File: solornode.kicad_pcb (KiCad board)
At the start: 2 copper layers, 35.9 x 42.4 mm, 86 parts, among them J1 Conn_01x06, J2 Conn_01x02, J3 Conn_01x02, J4 Conn_01x02, Q1 Q_NMOS_GDS, Q4 Q_PNP_BCE, Q5 Q_NPN_BCE, SW1 SW_Push, U1 LM358, U2 OC5864, U3 PY32F003F1xUx, U4 MAX485E, U5 SGM2033-3.3

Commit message: 修改元器件参数
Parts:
- C1: value 100u -> 22uF 50V
- C12, C13: value 100nF -> 100nF 100V
- C16: value C -> 10uF
- C17, C9: value 10u -> 10uF
- C2, C4: value 10u -> 2.2uF 100V
- C3: value 100u -> 10uF 100V
- C5: value 0.1u -> 0.1uF
- C6, C7: value 4.7n -> 4.7nF
- C8: value 2.2u -> 1uF 100V
- D12, D13: value D -> DSF1D
- D2, D3: value D_Zener -> CESD3V3D5
- D5, D6, D7: value ESD5Zxx -> CESDB5V0D3
- FB1, FB2: value 30 -> 1000R
- GD1, GD2, GD3: value GDT_2Pin -> 75V
- L2: value 47u -> 47uH
- L3: value L_Coupled -> 1000R
- Q1: value Q_NMOS_GDS -> AO3400
- Q4: value Q_PNP_BCE -> S8550
- Q5: value Q_NPN_BCE -> S8050
- R20, R26, R27: value R -> 10k
- R21, R22: value 22 -> 22R
- R28: value 470 -> 470R
- SW1: value SW_Push -> 3*4*2mm
- U3: value PY32F003F1xUx -> PY32F003F18U6TR
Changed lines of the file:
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@@
 			)
 		)
-		(property "Value" "R"
+		(property "Value" "10k"
 			(at 0 1.17 0)
 			(layer "F.Fab")
@@
 			)
 		)
-		(property "Value" "PY32F003F1xUx"
+		(property "Value" "PY32F003F18U6TR"
 			(at 0 2.83 0)
 			(layer "F.Fab")
@@
 			)
 		)
-		(property "Datasheet" ""
+		(property "Datasheet" "https://www.puyasemi.com/download_path/%E6%95%B0%E6%8D%AE%E6%89%8B%E5%86%8C/MCU%20%E5%BE%AE%E5%A4%84%E7%90%86%E5%99%A8/PY32F003%E7%B3%BB%E5%88%97%E6%95%B0%E6%8D%AE%E6%89%8B%E5%86%8C_V2.7.pdf"
 			(at 0 0 0)
 			(layer "F.Fab")
@@
 		(sheetname "根目录")
 		(sheetfile "solornode.kicad_sch")
-		(attr smd)
+		(attr smd dnp)
 		(fp_line
 			(start -1.685 0.96)
@@
 			)
 		)
-		(property "Value" "GDT_2Pin"
+		(property "Value" "75V"
 			(at 0 1.85 90)
 			(layer "F.Fab")
@@
 			)
 		)
-		(property "Value" "470"
+		(property "Value" "470R"
 			(at 0 1.17 0)
 			(layer "F.Fab")
@@
 			)
 		)
-		(property "Value" "Q_NMOS_GDS"
+		(property "Value" "AO3400"
 			(at 0 2.4 0)
 			(layer "F.Fab")
@@
 			)
 		)
-		(property "Value" "ESD5Zxx"
+		(property "Value" "CESDB5V0D3"
 			(at 0.1 1.9 0)
 			(layer "F.Fab")
@@
 			)
 		)
-		(property "Datasheet" "https://www.onsemi.com/pdf/datasheet/esd5z2.5t1-d.pdf"
+		(property "Datasheet" ""
 			(at 0 0 180)
 			(unlocked yes)
@@
 			)
 		)
-		(property "Value" "R"
+		(property "Value" "10k"
 			(at 0 1.17 90)
 			(layer "F.Fab")
@@
 			)
 		)
-		(property "Value" "100u"
+		(property "Value" "10uF 100V"
 			(at 0 4.35 90)
 			(layer "F.Fab")
@@
 			)
 		)
-		(property "Value" "100nF"
+		(property "Value" "100nF 100V"
 			(at 0 1.43 0)
 			(layer "F.Fab")
@@
 		(sheetname "根目录")
 		(sheetfile "solornode.kicad_sch")
-		(attr smd)
+		(attr smd dnp)
 		(fp_line
 			(start -0.237258 -0.5225)
@@
 			)
 		)
-		(property "Value" "100nF"
+		(property "Value" "100nF 100V"
 			(at 0 1.43 0)
 			(layer "F.Fab")
@@
 			)
 		)
-		(property "Datasheet" "http://www.ti.com/lit/ds/symlink/tlv700.pdf"
+		(property "Datasheet" "https://www.sg-micro.com/cn/product/SGM2033"
 			(at 0 0 0)
 			(layer "F.Fab")
@@
 			)
 		)
-		(property "Value" "47u"
+		(property "Value" "47uH"
 			(at 0 2.28 90)
 			(layer "F.Fab")
@@
 			)
 		)
-		(property "Value" "10u"
+		(property "Value" "10uF"
 			(at 0 1.68 90)
 			(layer "F.Fab")
@@
 			)
 		)
-		(property "Value" "10u"
+		(property "Value" "2.2uF 100V"
 			(at 0 2.3 90)
 			(layer "F.Fab")
@@
 			)
 		)
-		(property "Datasheet" "https://www.ti.com/lit/ds/symlink/lv2862.pdf"
+		(property "Datasheet" "http://ocxsemi.com/uploads/soft/20220426/1650943254.pdf"
 			(at 0 0 90)
 			(layer "F.Fab")
@@
 			)
 		)
-		(property "Value" "100u"
+		(property "Value" "22uF 50V"
 			(at 0 4.35 90)
 			(layer "F.Fab")
@@
 			)
 		)
-		(property "Value" "22"
+		(property "Value" "22R"
 			(at 0 1.43 0)
 			(layer "F.Fab")
@@
 			)
 		)
-		(property "Value" "30"
+		(property "Value" "1000R"
 			(at 0 1.43 0)
 			(layer "F.Fab")
@@
 			)
 		)
-		(property "Value" "2.2u"
+		(property "Value" "1uF 100V"
 			(at 0 1.68 90)
 			(layer "F.Fab")
@@
 			)
 		)
-		(property "Value" "10u"
+		(property "Value" "2.2uF 100V"
 			(at 0 2.3 90)
 			(layer "F.Fab")
@@
 		(sheetname "根目录")
 		(sheetfile "solornode.kicad_sch")
-		(attr smd)
+		(attr smd dnp)
 		(fp_line
 			(start -0.237258 0.5225)
@@
 			)
 		)
-		(property "Value" "22"
+		(property "Value" "22R"
 			(at 0 1.43 0)
 			(layer "F.Fab")
@@
 			)
 		)
-		(property "Value" "10u"
+		(property "Value" "10uF"
 			(at 0 1.68 0)
 			(layer "F.Fab")
@@
 			)
 		)
-		(property "Value" "ESD5Zxx"
+		(property "Value" "CESDB5V0D3"
 			(at 0.1 1.9 0)
 			(layer "F.Fab")
@@
 			)
 		)
-		(property "Datasheet" "https://www.onsemi.com/pdf/datasheet/esd5z2.5t1-d.pdf"
+		(property "Datasheet" ""
 			(at 0 0 180)
 			(unlocked yes)
@@
 			)
 		)
-		(property "Value" "C"
+		(property "Value" "10uF"
 			(at 0 1.68 90)
 			(layer "F.Fab")
@@
 			)
 		)
-		(property "Value" "ESD5Zxx"
+		(property "Value" "CESDB5V0D3"
 			(at 0.1 1.9 90)
 			(layer "F.Fab")
@@
 			)
 		)
-		(property "Datasheet" "https://www.onsemi.com/pdf/datasheet/esd5z2.5t1-d.pdf"
+		(property "Datasheet" ""
 			(at 0 0 90)
 			(unlocked yes)
@@
 		(sheetname "根目录")
 		(sheetfile "solornode.kicad_sch")
-		(attr smd)
+		(attr smd dnp)
 		(fp_line
 			(start -0.237258 -0.5225)
@@
 		(sheetname "根目录")
 		(sheetfile "solornode.kicad_sch")
-		(attr smd)
+		(attr smd dnp)
 		(fp_line
 			(start -0.227064 -0.735)
@@
 			)
 		)
-		(property "Value" "GDT_2Pin"
+		(property "Value" "75V"
 			(at 0 1.85 90)
 			(layer "F.Fab")
@@
 			)
 		)
-		(property "Value" "30"
+		(property "Value" "1000R"
 			(at 0 1.43 0)
 			(layer "F.Fab")
@@
 			)
 		)
-		(property "Value" "R"
+		(property "Value" "10k"
 			(at 0 1.17 90)
 			(layer "F.Fab")
@@
 			)
 		)
-		(property "Value" "L_Coupled"
+		(property "Value" "1000R"
 			(at 0 -4 90)
 			(layer "F.Fab")
@@
 			)
 		)
-		(property "Value" "SW_Push"
+		(property "Value" "3*4*2mm"
 			(at 0 2.5 90)
 			(layer "F.Fab")
@@
 			)
 		)
-		(property "Value" "GDT_2Pin"
+		(property "Value" "75V"
 			(at 0 1.85 90)
 			(layer "F.Fab")
@@
 			)
 		)
-		(property "Value" "D"
+		(property "Value" "DSF1D"
 			(at 0 2.1 90)
 			(layer "F.Fab")
@@
 			)
 		)
-		(property "Value" "Q_PNP_BCE"
+		(property "Value" "S8550"
 			(at 0 -2.4 0)
 			(layer "B.Fab")
@@
 			)
 		)
-		(property "Value" "4.7n"
+		(property "Value" "4.7nF"
 			(at 0 -1.16 90)
 			(layer "B.Fab")
@@
 			)
 		)
-		(property "Value" "0.1u"
+		(property "Value" "0.1uF"
 			(at 0 -1.16 0)
 			(layer "B.Fab")
@@
 			)
 		)
-		(property "Value" "D_Zener"
+		(property "Value" "CESD3V3D5"
 			(at 0 -1.4 90)
 			(layer "B.Fab")
@@
 			)
 		)
-		(property "Value" "4.7n"
+		(property "Value" "4.7nF"
 			(at 0 -1.16 90)
 			(layer "B.Fab")
@@
 			)
 		)
-		(property "Value" "D"
+		(property "Value" "DSF1D"
 			(at 0 -2.1 90)
 			(layer "B.Fab")
@@
 			)
 		)
-		(property "Value" "D_Zener"
+		(property "Value" "CESD3V3D5"
 			(at 0 -1.4 90)
 			(layer "B.Fab")
@@
 			)
 		)
-		(property "Value" "Q_NPN_BCE"
+		(property "Value" "S8050"
 			(at 0 -2.4 90)
 			(layer "B.Fab")

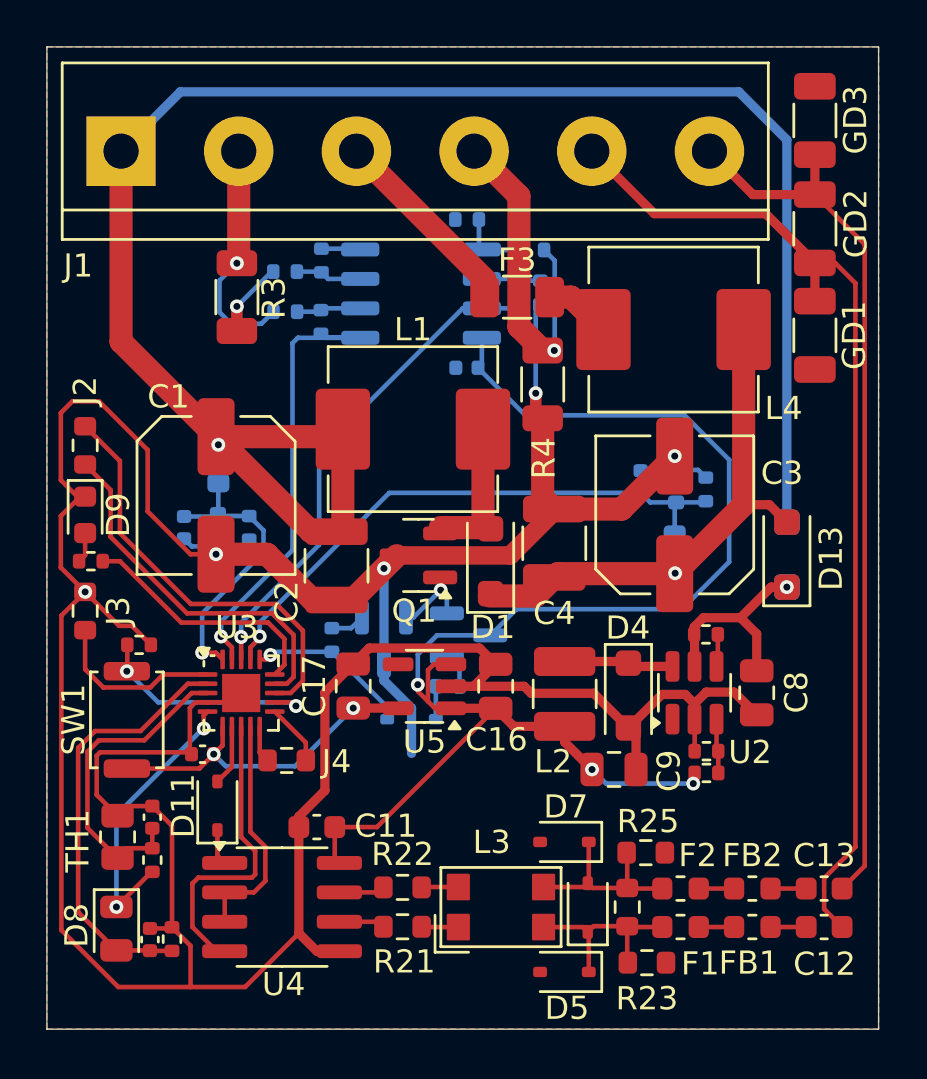
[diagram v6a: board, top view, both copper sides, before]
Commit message: 移除电源总线滤波电感
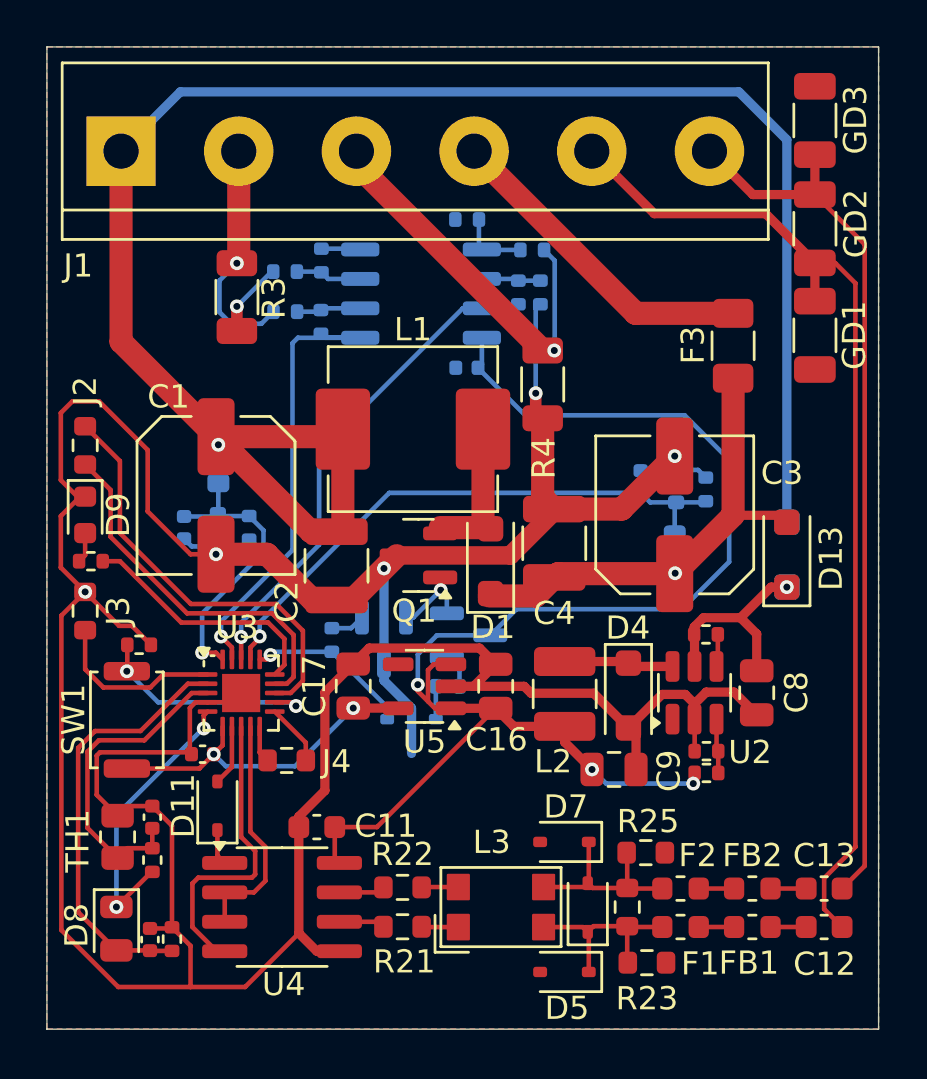
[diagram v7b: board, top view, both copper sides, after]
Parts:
- removed L4: 22uH, Inductor_SMD:L_APV_APH0630
- moved F3 9.55 mm to (142.2, 69.8), turned to -90 degrees
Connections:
- F3 pad 1: Net-(J1-Pin_3) -> Net-(J1-Pin_4)
- F3 pad 2: Net-(F3-Pad2) -> /BUS+
- J1 pad 3: Net-(J1-Pin_3) -> /BUS-
- J1 pad 4: /BUS- -> Net-(J1-Pin_4)
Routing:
- net Net-(J1-Pin_4): track 0.00 -> 14.1 mm
- net Net-(J1-Pin_3): track 8.59 -> 0.00 mm
- net Net-(F3-Pad2): track 2.90 -> 0.00 mm
- net /BUS-: track 14.4 -> 16.5 mm
- net /BUS+: track 22.3 -> 20.4 mm
